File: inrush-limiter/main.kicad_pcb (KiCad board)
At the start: 2 copper layers, 24 parts, among them K1 RELAY_2RT, P1 CONN_01X06, Q1 PN2222A, Q2 PN2222A, U1 LM393

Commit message: update
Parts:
- moved D5 117.6 mm to (214.6, 66.0), turned to 90 degrees
- moved R10 113.7 mm to (234.9, 104.1), turned to 180 degrees
- moved Q2 108.2 mm to (228.6, 54.6), turned to 270 degrees
- moved C3 102.6 mm to (203.2, 55.9), turned to 90 degrees
- moved R9 87.3 mm to (214.6, 50.8), turned to 90 degrees
- moved D4 74.3 mm to (183.5, 57.8), turned to 270 degrees
- moved D1 64.8 mm to (175.3, 44.5), turned to 270 degrees
- moved D3 63.8 mm to (175.9, 57.8), turned to 270 degrees
- moved K1 59.3 mm to (189.2, 121.9)
- moved D2 54.9 mm to (183.5, 43.8), turned to 270 degrees
- moved R7 47.7 mm to (168.9, 77.5), turned to 180 degrees
- moved R4 45.5 mm to (194.3, 88.9), turned to 90 degrees
- moved C2 40.1 mm to (158.8, 57.1), turned to 270 degrees
- moved R8 37.5 mm to (154.9, 133.3)
- moved F1 35.0 mm to (125.7, 61.0), turned to 180 degrees
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
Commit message: half-laid out
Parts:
- moved R2 75.8 mm to (120.7, 77.5)
- moved R4 68.3 mm to (127.0, 77.5), turned to 270 degrees
- moved R5 68.3 mm to (127.0, 88.9), turned to 270 degrees
- moved R10 66.1 mm to (168.9, 100.3)
- moved Q2 63.3 mm to (166.4, 43.2)
- moved D5 54.6 mm to (160.0, 64.8)
- moved R9 54.6 mm to (160.0, 50.8)
- moved C3 52.8 mm to (151.1, 47.0)
- moved R8 52.1 mm to (153.7, 81.3), turned to 180 degrees
- moved R1 46.6 mm to (108.0, 77.5)
- moved R7 46.4 mm to (123.2, 69.8)
- moved U1 45.8 mm to (133.3, 82.5)
- moved Q1 41.0 mm to (160.0, 83.8), turned to 90 degrees
- moved D2 40.0 mm to (143.5, 43.2)
- moved D4 40.0 mm to (143.5, 57.1)
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
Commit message: update
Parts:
- moved D1 25.4 mm to (139.7, 68.6), turned to 90 degrees
- moved D2 25.4 mm to (143.5, 68.6), turned to 90 degrees
- moved D5 20.4 mm to (158.8, 44.5), turned to 270 degrees
- moved K1 15.3 mm to (176.5, 90.2)
- moved Q2 8.98 mm to (165.1, 52.1), turned to 90 degrees
- moved R9 8.98 mm to (158.8, 59.7), turned to 270 degrees
- moved Q1 4.02 mm to (158.8, 80.0), turned to 270 degrees
- moved D3 2.54 mm to (139.7, 54.6), turned to 90 degrees
- moved D4 2.54 mm to (143.5, 54.6), turned to 90 degrees
- moved C3 1.27 mm to (151.1, 45.7), turned to 270 degrees
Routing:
- net +5V: track 0.00 -> 121.8 mm
- net GND: track 0.00 -> 56.2 mm
- net Net-(D2-Pad2): track 0.00 -> 45.8 mm
- net AC-live: track 0.00 -> 35.7 mm
- net Net-(C2-Pad1): track 0.00 -> 29.9 mm
- net Net-(D5-Pad2): track 0.00 -> 18.8 mm
- net AC-live-f: track 0.00 -> 15.7 mm
- net AC-neut: track 0.00 -> 2.54 mm
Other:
- net class Default: clearance 0.2 -> 0.25; trace_width 0.25 -> 1
- rule trace_clearance: 0.2 -> 0.25

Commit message: update
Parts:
- moved R10 37.0 mm to (132.1, 104.1)
- turned F1 to 90 degrees
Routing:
- net GND: track 56.2 -> 138.0 mm
- net Net-(R8-Pad2): track 0.00 -> 34.6 mm
- net AC-neut: track 2.54 -> 32.8 mm
- net Net-(C1-Pad1): track 0.00 -> 29.8 mm
- net Net-(K1-Pad9): track 0.00 -> 29.7 mm
- net +5V: track 121.8 -> 96.7 mm
- net AC-live: track 35.7 -> 11.7 mm
- net Net-(R4-Pad2): track 0.00 -> 10.2 mm
- net AC-live-f: track 15.7 -> 6.45 mm
- net Net-(Q1-Pad2): track 0.00 -> 5.08 mm
- net Net-(D2-Pad2): track 45.8 -> 48.9 mm
- net Net-(C2-Pad1): track 29.9 -> 32.9 mm

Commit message: update
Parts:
- moved R10 11.5 mm to (120.7, 102.9)
- moved Q1 1.80 mm to (160.0, 78.7)
- moved R5 1.80 mm to (128.3, 87.6)
- moved C1 1.80 mm to (115.6, 92.7)
- moved R3 1.80 mm to (121.9, 87.6)
- moved R4 1.80 mm to (128.3, 76.2)
- moved R8 1.80 mm to (154.9, 80.0)
- moved U1 1.80 mm to (134.6, 81.3)
- moved R1 1.80 mm to (109.2, 76.2)
- moved R2 1.80 mm to (121.9, 76.2)
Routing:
- net GND: track 138.0 -> 178.9 mm
- net AC-live-f: track 6.45 -> 33.5 mm
- net +5V: track 96.7 -> 112.8 mm
- net AC-neut: track 32.8 -> 28.5 mm
- net AC-live: track 11.7 -> 10.4 mm
- net Net-(C1-Pad1): track 29.8 -> 30.6 mm
- added copper zone on B.Cu, net GND

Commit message: update
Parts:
- moved K1 5.39 mm to (180.3, 94.0)
- moved C1 2.54 mm to (118.1, 92.7)
- moved R1 2.54 mm to (111.8, 76.2)
- moved Q1 2.54 mm to (162.6, 78.7)
- moved R2 2.54 mm to (124.5, 76.2)
- moved R3 2.54 mm to (124.5, 87.6)
- moved R4 2.54 mm to (130.8, 76.2)
- moved R5 2.54 mm to (130.8, 87.6)
- moved R8 2.54 mm to (157.5, 80.0)
- moved U1 2.54 mm to (137.2, 81.3)
- moved R10 1.80 mm to (119.4, 104.1)
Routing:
- net GND: track 178.9 -> 188.0 mm
- net +5V: track 112.8 -> 104.8 mm
- net Net-(D2-Pad2): track 48.9 -> 47.1 mm
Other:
- board text added: "Hi Voltage"

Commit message: update
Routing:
- net GND: track 188.0 -> 185.5 mm
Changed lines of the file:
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@@
     (thickness 1.6)
     (drawings 1)
-    (tracks 116)
+    (tracks 115)
     (zones 0)
     (modules 24)
@@
   (segment (start 127 90.17) (end 133.35 90.17) (width 1) (layer B.Cu) (net 1))
   (segment (start 124.46 83.82) (end 124.46 87.63) (width 1) (layer B.Cu) (net 1))
-  (segment (start 162.56 78.74) (end 162.56 74.93) (width 1) (layer B.Cu) (net 2))
-  (segment (start 157.48 74.93) (end 157.48 68.58) (width 1) (layer B.Cu) (net 2))
-  (segment (start 162.56 74.93) (end 157.48 74.93) (width 1) (layer B.Cu) (net 2))
+  (segment (start 158.75 67.31) (end 160.02 68.58) (width 1) (layer B.Cu) (net 2) (status 400000))
+  (segment (start 162.56 68.58) (end 162.56 78.74) (width 1) (layer B.Cu) (net 2) (status 800000))
+  (segment (start 160.02 68.58) (end 162.56 68.58) (width 1) (layer B.Cu) (net 2))
   (segment (start 109.22 64.77) (end 109.22 78.74) (width 1) (layer B.Cu) (net 2))
   (segment (start 114.3 81.28) (end 114.3 85.09) (width 1) (layer B.Cu) (net 2))
@@
   (segment (start 106.68 67.31) (end 109.22 64.77) (width 1) (layer B.Cu) (net 2))
   (segment (start 137.16 88.9) (end 137.16 95.25) (width 1) (layer B.Cu) (net 2))
-  (segment (start 158.75 67.31) (end 160.02 68.58) (width 1) (layer B.Cu) (net 2))
   (segment (start 162.56 78.74) (end 163.83 78.74) (width 1) (layer B.Cu) (net 2))
+  (segment (start 157.48 95.25) (end 137.16 95.25) (width 1) (layer B.Cu) (net 2))
+  (segment (start 165.1 87.63) (end 157.48 95.25) (width 1) (layer B.Cu) (net 2))
+  (segment (start 165.1 80.01) (end 165.1 87.63) (width 1) (layer B.Cu) (net 2))
   (segment (start 163.83 78.74) (end 165.1 80.01) (width 1) (layer B.Cu) (net 2))
-  (segment (start 165.1 80.01) (end 165.1 87.63) (width 1) (layer B.Cu) (net 2))
-  (segment (start 165.1 87.63) (end 157.48 95.25) (width 1) (layer B.Cu) (net 2))
-  (segment (start 157.48 95.25) (end 137.16 95.25) (width 1) (layer B.Cu) (net 2))
   (segment (start 137.16 95.25) (end 130.81 95.25) (width 1) (layer B.Cu) (net 2))
   (segment (start 118.11 95.21) (end 124.42 95.21) (width 1) (layer B.Cu) (net 2))

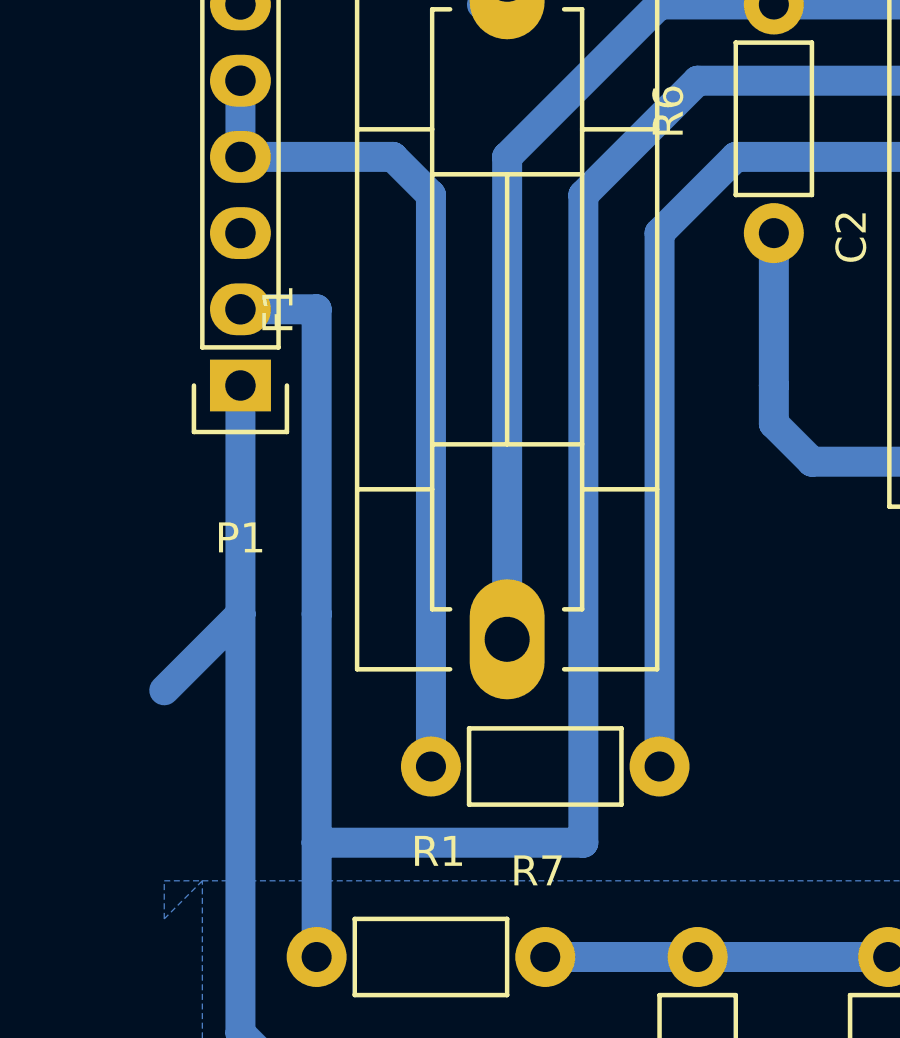
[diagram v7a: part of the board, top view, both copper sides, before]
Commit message: fix relay footprint and reimport
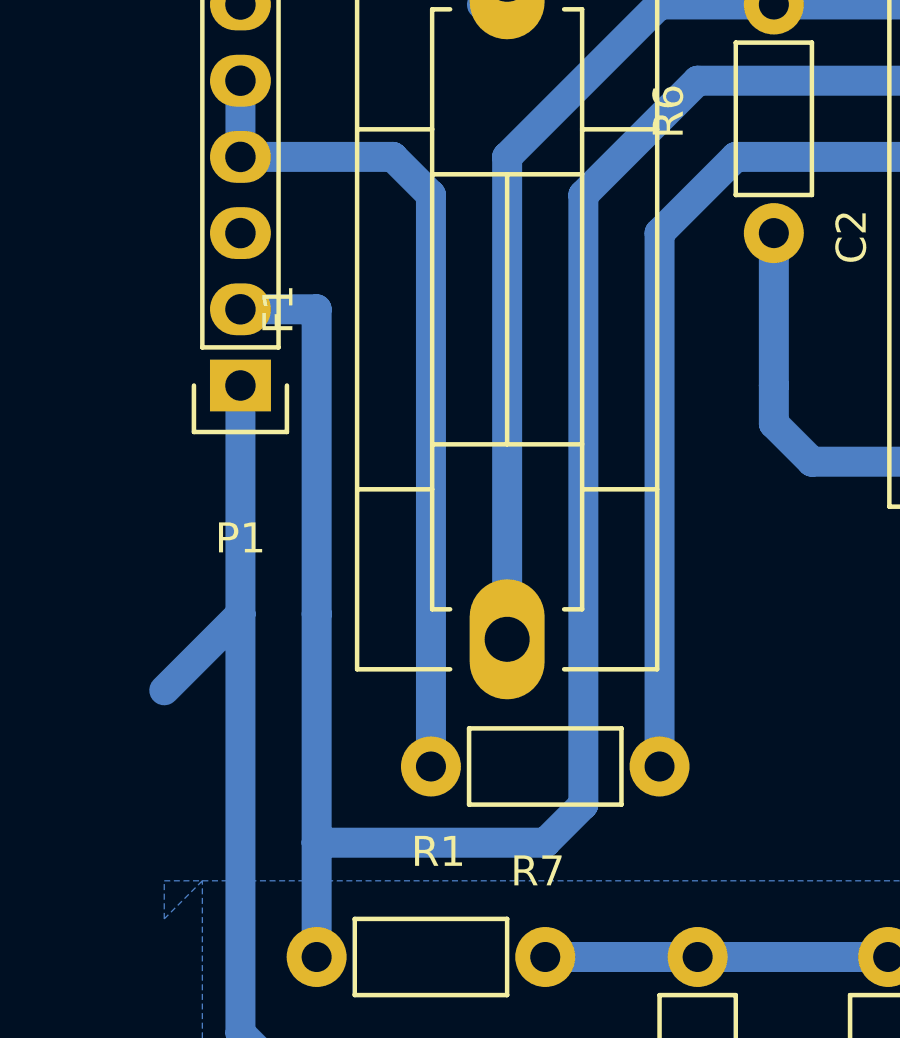
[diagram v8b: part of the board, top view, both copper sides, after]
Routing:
- net +5V: track 104.8 -> 104.1 mm
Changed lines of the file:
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@@
     (thickness 1.6)
     (drawings 1)
-    (tracks 115)
+    (tracks 116)
     (zones 0)
     (modules 24)
@@
   (segment (start 127 44.45) (end 133.11 44.45) (width 1) (layer B.Cu) (net 4))
   (segment (start 133.11 44.45) (end 133.35 44.69) (width 1) (layer B.Cu) (net 4))
+  (segment (start 120.65 50.8) (end 120.65 71.12) (width 1) (layer B.Cu) (net 5))
+  (segment (start 138.43052 44.44948) (end 137.16 45.72) (width 1) (layer B.Cu) (net 5))
+  (segment (start 124.46 46.99) (end 120.65 50.8) (width 1) (layer B.Cu) (net 5))
+  (segment (start 135.89 46.99) (end 124.46 46.99) (width 1) (layer B.Cu) (net 5))
+  (segment (start 137.16 45.72) (end 135.89 46.99) (width 1) (layer B.Cu) (net 5))
+  (segment (start 139.69746 44.44948) (end 138.43052 44.44948) (width 1) (layer B.Cu) (net 5))
+  (segment (start 119.38 72.39) (end 111.76 72.39) (width 1) (layer B.Cu) (net 5))
+  (segment (start 120.65 71.12) (end 119.38 72.39) (width 1) (layer B.Cu) (net 5))
   (segment (start 111.76 76.2) (end 111.76 72.39) (width 1) (layer B.Cu) (net 5))
   (segment (start 111.76 64.77) (end 111.76 72.39) (width 1) (layer B.Cu) (net 5))
-  (segment (start 139.69746 44.44948) (end 138.43052 44.44948) (width 1) (layer B.Cu) (net 5))
-  (segment (start 137.16 45.72) (end 135.89 46.99) (width 1) (layer B.Cu) (net 5))
-  (segment (start 135.89 46.99) (end 124.46 46.99) (width 1) (layer B.Cu) (net 5))
-  (segment (start 124.46 46.99) (end 120.65 50.8) (width 1) (layer B.Cu) (net 5))
-  (segment (start 120.65 50.8) (end 120.65 72.39) (width 1) (layer B.Cu) (net 5))
-  (segment (start 120.65 72.39) (end 111.76 72.39) (width 1) (layer B.Cu) (net 5))
-  (segment (start 138.43052 44.44948) (end 137.16 45.72) (width 1) (layer B.Cu) (net 5))
+  (segment (start 111.76 54.61) (end 109.22 54.61) (width 1) (layer B.Cu) (net 5))
+  (segment (start 111.76 64.77) (end 111.76 54.61) (width 1) (layer B.Cu) (net 5))
   (segment (start 139.69746 44.44948) (end 139.69746 44.44746) (width 1) (layer B.Cu) (net 5))
-  (segment (start 111.76 64.77) (end 111.76 54.61) (width 1) (layer B.Cu) (net 5))
-  (segment (start 111.76 54.61) (end 109.22 54.61) (width 1) (layer B.Cu) (net 5))
   (segment (start 158.75254 44.45052) (end 160.02052 44.45052) (width 1) (layer B.Cu) (net 5))
   (segment (start 160.02052 44.45052) (end 165.1 49.53) (width 1) (layer B.Cu) (net 5))
